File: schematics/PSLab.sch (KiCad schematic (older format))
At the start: 183 parts, among them J1 DoublePins, J11 Li-Ion Battery, J2 Power Pins, J3 Wave Generator, J4 I2C, J5 I2C, J6 ESP01, J7 UART, J9 SPI, P1 SDCard, Q1 MMBT3906, Q2 MMBT3904, Q3 MMBT3906, Q4 Q_NMOS_DGS, SW1 BOOT, SW2 MCLR Reset, SW3 USB_C - Generic, U1 LDFM33PUR, U10 TL082, U11 TL082, U12 MCP4728, U13 MCP6S21, U14 MCP6S21, U15 CP2102N, U16 SP0503BAHT, U18 LTC4040, U19 TC1240A, U2 74HC126, U3 PIC24EP256GP204, U4 DS1307Z+, U5 TC7660, U7 LM324, U8 TL082, U9 TL082, X2 32.768 kHz, Y1 12 MHz

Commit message: fix: osc signal routes
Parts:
- BT1: footprint Battery:BatteryHolder_LINX_BAT-HLD-012-SMT -> PSLab:BatteryHolder_LINX_BAT-HLD-012-SMT
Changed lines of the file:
@@
 Data
 89 50 4E 47 0D 0A 1A 0A 00 00 00 0D 49 48 44 52 00 00 02 08 00 00 00 CC 08 03 00 00 00 21 C4 AB
-DA 00 00 00 03 73 42 49 54 08 08 08 DB E1 4F E0 00 00 03 00 50 4C 54 45 02 00 00 FF FF E2 79 5D
+DA 00 00 00 03 73 42 49 54 08 08 08 DB E1 4F E0 00 00 03 00 50 4C 54 45 01 00 00 FF FF E2 79 5D
 9D 28 5D A5 28 7D CE E2 FF FF 81 5D B6 A5 EA FF C6 99 A5 28 99 E2 FF EA D6 59 5D C2 C6 FF FF 59
 B6 F2 FF FF F2 A5 7D A5 28 5D C6 E2 B6 B6 81 CE FF FF CE C6 81 7D D6 55 5D A1 59 7D BE F6 F6 F6
@@
 F6 99 D2 CE 40 9D D6 EA EE F6 40 5D A5 28 5D BA 7D D2 DE 55 AE DE 28 75 C2 CA DA EA 99 AA B6 65
 C2 DE 85 A5 CA 4C 4C 4C A1 A1 A1 3C 3C 3C 61 65 69 A5 B2 BE 85 A1 CE 91 99 A1 EE F2 F2 7D 81 81
-B6 BE C6 91 91 91 7D 7D 81 50 79 B6 C2 C2 C2 99 B2 7D 5D B6 DE FA FA FA 4A AB 90 C2 00 00 00 01
+B6 BE C6 91 91 91 7D 7D 81 50 79 B6 C2 C2 C2 99 B2 7D 5D B6 DE FA FA FA 76 CF DF 8C 00 00 00 01
 74 52 4E 53 00 40 E6 D8 66 00 00 15 08 49 44 41 54 78 9C ED 9D 7B 80 15 D5 79 C0 67 99 A5 31 A6
 26 05 83 EC 2E FB 76 60 9B 44 F6 01 BB CA 43 77 F7 C6 18 1F 10 31 36 1B 5D 4C 82 69 D6 24 D6 A0
@@
 F 0 "BT1" V 11150 7276 50  0000 C CNN
 F 1 "CR1225" V 11251 7086 50  0000 C CNN
-F 2 "Battery:BatteryHolder_LINX_BAT-HLD-012-SMT" V 11100 7085 50  0001 C CNN
+F 2 "PSLab:BatteryHolder_LINX_BAT-HLD-012-SMT" V 11100 7085 50  0001 C CNN
 F 3 "https://eu.mouser.com/datasheet/2/238/bat-hld-012-smt-1659340.pdf" V 11100 7085 50  0001 C CNN
 F 4 "Coin cell battery holder (CR1225/1216)" V 11100 7025 50  0001 C CNN "Description"

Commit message: refactor: global track refresh
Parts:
- U1: footprint Package_DFN_QFN:DFN-6-1EP_3x3mm_P0.95mm_EP1.7x2.6mm -> PSLab:DFN-6-1EP_3x3mm_P0.95mm_EP1.7x2.6mm
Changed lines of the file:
@@
 Data
 89 50 4E 47 0D 0A 1A 0A 00 00 00 0D 49 48 44 52 00 00 02 08 00 00 00 CC 08 03 00 00 00 21 C4 AB
-DA 00 00 00 03 73 42 49 54 08 08 08 DB E1 4F E0 00 00 03 00 50 4C 54 45 01 00 00 FF FF E2 79 5D
+DA 00 00 00 03 73 42 49 54 08 08 08 DB E1 4F E0 00 00 03 00 50 4C 54 45 02 00 00 FF FF E2 79 5D
 9D 28 5D A5 28 7D CE E2 FF FF 81 5D B6 A5 EA FF C6 99 A5 28 99 E2 FF EA D6 59 5D C2 C6 FF FF 59
 B6 F2 FF FF F2 A5 7D A5 28 5D C6 E2 B6 B6 81 CE FF FF CE C6 81 7D D6 55 5D A1 59 7D BE F6 F6 F6
@@
 F6 99 D2 CE 40 9D D6 EA EE F6 40 5D A5 28 5D BA 7D D2 DE 55 AE DE 28 75 C2 CA DA EA 99 AA B6 65
 C2 DE 85 A5 CA 4C 4C 4C A1 A1 A1 3C 3C 3C 61 65 69 A5 B2 BE 85 A1 CE 91 99 A1 EE F2 F2 7D 81 81
-B6 BE C6 91 91 91 7D 7D 81 50 79 B6 C2 C2 C2 99 B2 7D 5D B6 DE FA FA FA 76 CF DF 8C 00 00 00 01
+B6 BE C6 91 91 91 7D 7D 81 50 79 B6 C2 C2 C2 99 B2 7D 5D B6 DE FA FA FA 4A AB 90 C2 00 00 00 01
 74 52 4E 53 00 40 E6 D8 66 00 00 15 08 49 44 41 54 78 9C ED 9D 7B 80 15 D5 79 C0 67 99 A5 31 A6
 26 05 83 EC 2E FB 76 60 9B 44 F6 01 BB CA 43 77 F7 C6 18 1F 10 31 36 1B 5D 4C 82 69 D6 24 D6 A0
@@
 F 0 "U1" H 6900 4400 50  0000 C CNN
 F 1 "LDFM33PUR" H 7295 4400 50  0000 C CNN
-F 2 "Package_DFN_QFN:DFN-6-1EP_3x3mm_P0.95mm_EP1.7x2.6mm" H 7200 4200 60  0001 C CNN
+F 2 "PSLab:DFN-6-1EP_3x3mm_P0.95mm_EP1.7x2.6mm" H 7200 4200 60  0001 C CNN
 F 3 "https://eu.mouser.com/datasheet/2/389/dm00063302-1797750.pdf" H 7200 4200 60  0001 C CNN
 F 4 "DFN-6-1EP_3x3mm_Pitch0.95mm" H 7200 4200 50  0001 C CNN "Description"

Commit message: upgrade: lm324 to tssop14
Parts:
- U7: footprint Package_SO:SOIC-14_3.9x8.7mm_P1.27mm -> Package_SO:TSSOP-14_4.4x5mm_P0.65mm; Description SOIC 14 -> TSSOP-14; Mfr No. LM324D -> LM324APT; PartNumber LM324D -> LM324APT; Price (none) -> 0.45
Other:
- note added: "01"
- note added: "02"
- note added: "03"
- note added: "04"
- note added: "Oscilloscope Channel 01"
- note added: "Oscilloscope Channel 02"
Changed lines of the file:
@@
 Data
 89 50 4E 47 0D 0A 1A 0A 00 00 00 0D 49 48 44 52 00 00 02 08 00 00 00 CC 08 03 00 00 00 21 C4 AB
-DA 00 00 00 03 73 42 49 54 08 08 08 DB E1 4F E0 00 00 03 00 50 4C 54 45 02 00 00 FF FF E2 79 5D
+DA 00 00 00 03 73 42 49 54 08 08 08 DB E1 4F E0 00 00 03 00 50 4C 54 45 01 00 00 FF FF E2 79 5D
 9D 28 5D A5 28 7D CE E2 FF FF 81 5D B6 A5 EA FF C6 99 A5 28 99 E2 FF EA D6 59 5D C2 C6 FF FF 59
 B6 F2 FF FF F2 A5 7D A5 28 5D C6 E2 B6 B6 81 CE FF FF CE C6 81 7D D6 55 5D A1 59 7D BE F6 F6 F6
@@
 F6 99 D2 CE 40 9D D6 EA EE F6 40 5D A5 28 5D BA 7D D2 DE 55 AE DE 28 75 C2 CA DA EA 99 AA B6 65
 C2 DE 85 A5 CA 4C 4C 4C A1 A1 A1 3C 3C 3C 61 65 69 A5 B2 BE 85 A1 CE 91 99 A1 EE F2 F2 7D 81 81
-B6 BE C6 91 91 91 7D 7D 81 50 79 B6 C2 C2 C2 99 B2 7D 5D B6 DE FA FA FA 4A AB 90 C2 00 00 00 01
+B6 BE C6 91 91 91 7D 7D 81 50 79 B6 C2 C2 C2 99 B2 7D 5D B6 DE FA FA FA 76 CF DF 8C 00 00 00 01
 74 52 4E 53 00 40 E6 D8 66 00 00 15 08 49 44 41 54 78 9C ED 9D 7B 80 15 D5 79 C0 67 99 A5 31 A6
 26 05 83 EC 2E FB 76 60 9B 44 F6 01 BB CA 43 77 F7 C6 18 1F 10 31 36 1B 5D 4C 82 69 D6 24 D6 A0
@@
 F 0 "U7" H 21175 3075 50  0000 C CNN
 F 1 "LM324" H 21125 2900 50  0000 C CNN
-F 2 "Package_SO:SOIC-14_3.9x8.7mm_P1.27mm" H 21125 3000 50  0001 C CNN
-F 3 "http://www.ti.com/general/docs/suppproductinfo.tsp?distId=26&gotoUrl=http%3A%2F%2Fwww.ti.com%2Flit%2Fgpn%2FLM324" H 21225 3100 50  0001 C CNN
-F 4 "LM324D" H 21175 2900 50  0001 C CNN "PartNumber"
-F 5 "SOIC 14" H 21175 2900 50  0001 C CNN "Description"
-F 6 "LM324D" H 21175 2900 50  0001 C CNN "Mfr No."
+F 2 "Package_SO:TSSOP-14_4.4x5mm_P0.65mm" H 21125 3000 50  0001 C CNN
+F 3 "https://eu.mouser.com/datasheet/2/389/cd00001046-1795623.pdf" H 21225 3100 50  0001 C CNN
+F 4 "LM324APT" H 21175 2900 50  0001 C CNN "PartNumber"
+F 5 "TSSOP-14" H 21175 2900 50  0001 C CNN "Description"
+F 6 "LM324APT" H 21175 2900 50  0001 C CNN "Mfr No."
+F 7 "0.45" H 21175 2900 50  0001 C CNN "Price"
 	1    21175 2900
 	1    0    0    -1
@@
 F 0 "U7" H 21175 2100 50  0000 C CNN
 F 1 "LM324" H 21100 1925 50  0000 C CNN
-F 2 "Package_SO:SOIC-14_3.9x8.7mm_P1.27mm" H 21100 2025 50  0001 C CNN
-F 3 "http://www.ti.com/general/docs/suppproductinfo.tsp?distId=26&gotoUrl=http%3A%2F%2Fwww.ti.com%2Flit%2Fgpn%2FLM324" H 21200 2125 50  0001 C CNN
-F 4 "SOIC 14" H 21150 1925 50  0001 C CNN "Description"
-F 5 "LM324D" H 21150 1925 50  0001 C CNN "Mfr No."
-F 6 "LM324D" H 21150 1925 50  0001 C CNN "PartNumber"
+F 2 "Package_SO:TSSOP-14_4.4x5mm_P0.65mm" H 21100 2025 50  0001 C CNN
+F 3 "https://eu.mouser.com/datasheet/2/389/cd00001046-1795623.pdf" H 21200 2125 50  0001 C CNN
+F 4 "TSSOP-14" H 21150 1925 50  0001 C CNN "Description"
+F 5 "LM324APT" H 21150 1925 50  0001 C CNN "Mfr No."
+F 6 "LM324APT" H 21150 1925 50  0001 C CNN "PartNumber"
+F 7 "0.45" H 21150 1925 50  0001 C CNN "Price"
 	2    21150 1925
 	1    0    0    -1
@@
 F 0 "U7" H 21175 1175 50  0000 C CNN
 F 1 "LM324" H 21100 1350 50  0000 C CNN
-F 2 "Package_SO:SOIC-14_3.9x8.7mm_P1.27mm" H 21100 1450 50  0001 C CNN
-F 3 "http://www.ti.com/general/docs/suppproductinfo.tsp?distId=26&gotoUrl=http%3A%2F%2Fwww.ti.com%2Flit%2Fgpn%2FLM324" H 21200 1550 50  0001 C CNN
-F 4 "SOIC 14" H 21150 1350 50  0001 C CNN "Description"
-F 5 "LM324D" H 21150 1350 50  0001 C CNN "Mfr No."
-F 6 "LM324D" H 21150 1350 50  0001 C CNN "PartNumber"
+F 2 "Package_SO:TSSOP-14_4.4x5mm_P0.65mm" H 21100 1450 50  0001 C CNN
+F 3 "https://eu.mouser.com/datasheet/2/389/cd00001046-1795623.pdf" H 21200 1550 50  0001 C CNN
+F 4 "TSSOP-14" H 21150 1350 50  0001 C CNN "Description"
+F 5 "LM324APT" H 21150 1350 50  0001 C CNN "Mfr No."
+F 6 "LM324APT" H 21150 1350 50  0001 C CNN "PartNumber"
+F 7 "0.45" H 21150 1350 50  0001 C CNN "Price"
 	3    21150 1350
 	1    0    0    1
@@
 F 0 "U7" H 22050 3075 50  0000 C CNN
 F 1 "LM324" H 21975 2900 50  0000 C CNN
-F 2 "Package_SO:SOIC-14_3.9x8.7mm_P1.27mm" H 21975 3000 50  0001 C CNN
-F 3 "http://www.ti.com/general/docs/suppproductinfo.tsp?distId=26&gotoUrl=http%3A%2F%2Fwww.ti.com%2Flit%2Fgpn%2FLM324" H 22075 3100 50  0001 C CNN
-F 4 "SOIC 14" H 22025 2900 50  0001 C CNN "Description"
-F 5 "LM324D" H 22025 2900 50  0001 C CNN "Mfr No."
-F 6 "LM324D" H 22025 2900 50  0001 C CNN "PartNumber"
+F 2 "Package_SO:TSSOP-14_4.4x5mm_P0.65mm" H 21975 3000 50  0001 C CNN
+F 3 "https://eu.mouser.com/datasheet/2/389/cd00001046-1795623.pdf" H 22075 3100 50  0001 C CNN
+F 4 "TSSOP-14" H 22025 2900 50  0001 C CNN "Description"
+F 5 "LM324APT" H 22025 2900 50  0001 C CNN "Mfr No."
+F 6 "LM324APT" H 22025 2900 50  0001 C CNN "PartNumber"
+F 7 "0.45" H 22025 2900 50  0001 C CNN "Price"
 	4    22025 2900
 	1    0    0    -1
@@
 F 0 "U7" V 19525 2875 50  0000 C CNN
 F 1 "LM324" V 19800 2875 50  0000 C CNN
-F 2 "Package_SO:SOIC-14_3.9x8.7mm_P1.27mm" H 19725 2975 50  0001 C CNN
-F 3 "http://www.ti.com/general/docs/suppproductinfo.tsp?distId=26&gotoUrl=http%3A%2F%2Fwww.ti.com%2Flit%2Fgpn%2FLM324" H 19825 3075 50  0001 C CNN
-F 4 "SOIC 14" H 19775 2875 50  0001 C CNN "Description"
-F 5 "LM324D" H 19775 2875 50  0001 C CNN "Mfr No."
-F 6 "LM324D" H 19775 2875 50  0001 C CNN "PartNumber"
+F 2 "Package_SO:TSSOP-14_4.4x5mm_P0.65mm" H 19725 2975 50  0001 C CNN
+F 3 "https://eu.mouser.com/datasheet/2/389/cd00001046-1795623.pdf" H 19825 3075 50  0001 C CNN
+F 4 "TSSOP-14" H 19775 2875 50  0001 C CNN "Description"
+F 5 "LM324APT" H 19775 2875 50  0001 C CNN "Mfr No."
+F 6 "LM324APT" H 19775 2875 50  0001 C CNN "PartNumber"
+F 7 "0.45" H 19775 2875 50  0001 C CNN "Price"
 	5    19775 2875
 	0    1    1    0
@@
 	0    -1   -1   0
 $EndComp
+Text Notes 19000 6050 0    39   ~ 8
+Oscilloscope Channel 02
+Text Notes 15050 6050 0    39   ~ 8
+Oscilloscope Channel 01
+Text Notes 15075 8350 0    79   ~ 16
+01
+Wire Notes Line style solid rgb(255, 0, 0)
+	15025 8175 15300 8175
+Wire Notes Line style solid rgb(255, 0, 0)
+	15300 8175 15300 8425
+Text Notes 19025 8350 0    79   ~ 16
+02
+Wire Notes Line style solid rgb(255, 0, 0)
+	18975 8175 19250 8175
+Wire Notes Line style solid rgb(255, 0, 0)
+	19250 8175 19250 8425
+Text Notes 18475 5725 0    79   ~ 16
+03
+Wire Notes Line style solid rgb(255, 0, 0)
+	18425 5550 18700 5550
+Wire Notes Line style solid rgb(255, 0, 0)
+	18700 5550 18700 5800
+Text Notes 15075 5725 0    79   ~ 16
+04
+Wire Notes Line style solid rgb(255, 0, 0)
+	15025 5550 15300 5550
+Wire Notes Line style solid rgb(255, 0, 0)
+	15300 5550 15300 5800
 $EndSCHEMATC

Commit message: refactor: osc placement
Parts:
- U2: footprint Package_SO:SOIC-14_3.9x8.7mm_P1.27mm -> Package_SO:TSSOP-14_4.4x5mm_P0.65mm; Description (none) -> TSSOP-14; Mfr No. (none) -> SN74HC126PW; PartNumber (none) -> SN74HC126PW; Price (none) -> 0.42
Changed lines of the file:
@@
 F 0 "U2" H 10575 9492 39  0000 C CNN
 F 1 "74HC126" H 10575 9575 50  0000 C CNN
-F 2 "Package_SO:SOIC-14_3.9x8.7mm_P1.27mm" H 10575 9275 50  0001 C CNN
-F 3 "https://eu.mouser.com/datasheet/2/408/74HC126D_datasheet_en_20160804-959200.pdf" H 10575 9275 50  0001 C CNN
+F 2 "Package_SO:TSSOP-14_4.4x5mm_P0.65mm" H 10575 9275 50  0001 C CNN
+F 3 "http://www.ti.com/general/docs/suppproductinfo.tsp?distId=26&gotoUrl=http%3A%2F%2Fwww.ti.com%2Flit%2Fgpn%2Fsn74hc126" H 10575 9275 50  0001 C CNN
+F 4 "TSSOP-14" H 10575 9275 50  0001 C CNN "Description"
+F 5 "SN74HC126PW" H 10575 9275 50  0001 C CNN "Mfr No."
+F 6 "SN74HC126PW" H 10575 9275 50  0001 C CNN "PartNumber"
+F 7 "0.42" H 10575 9275 50  0001 C CNN "Price"
 	1    10575 9275
 	1    0    0    1
@@
 F 0 "U2" H 11725 9492 39  0000 C CNN
 F 1 "74HC126" H 11725 9575 50  0000 C CNN
-F 2 "Package_SO:SOIC-14_3.9x8.7mm_P1.27mm" H 11725 9275 50  0001 C CNN
-F 3 "https://eu.mouser.com/datasheet/2/408/74HC126D_datasheet_en_20160804-959200.pdf" H 11725 9275 50  0001 C CNN
+F 2 "Package_SO:TSSOP-14_4.4x5mm_P0.65mm" H 11725 9275 50  0001 C CNN
+F 3 "http://www.ti.com/general/docs/suppproductinfo.tsp?distId=26&gotoUrl=http%3A%2F%2Fwww.ti.com%2Flit%2Fgpn%2Fsn74hc126" H 11725 9275 50  0001 C CNN
+F 4 "TSSOP-14" H 11725 9275 50  0001 C CNN "Description"
+F 5 "SN74HC126PW" H 11725 9275 50  0001 C CNN "Mfr No."
+F 6 "SN74HC126PW" H 11725 9275 50  0001 C CNN "PartNumber"
+F 7 "0.42" H 11725 9275 50  0001 C CNN "Price"
 	2    11725 9275
 	1    0    0    1
@@
 F 0 "U2" H 11725 10617 39  0000 C CNN
 F 1 "74HC126" H 11725 10700 50  0000 C CNN
-F 2 "Package_SO:SOIC-14_3.9x8.7mm_P1.27mm" H 11725 10400 50  0001 C CNN
-F 3 "https://eu.mouser.com/datasheet/2/408/74HC126D_datasheet_en_20160804-959200.pdf" H 11725 10400 50  0001 C CNN
+F 2 "Package_SO:TSSOP-14_4.4x5mm_P0.65mm" H 11725 10400 50  0001 C CNN
+F 3 "http://www.ti.com/general/docs/suppproductinfo.tsp?distId=26&gotoUrl=http%3A%2F%2Fwww.ti.com%2Flit%2Fgpn%2Fsn74hc126" H 11725 10400 50  0001 C CNN
+F 4 "TSSOP-14" H 11725 10400 50  0001 C CNN "Description"
+F 5 "SN74HC126PW" H 11725 10400 50  0001 C CNN "Mfr No."
+F 6 "SN74HC126PW" H 11725 10400 50  0001 C CNN "PartNumber"
+F 7 "0.42" H 11725 10400 50  0001 C CNN "Price"
 	3    11725 10400
 	1    0    0    1
@@
 F 0 "U2" H 10575 10617 39  0000 C CNN
 F 1 "74HC126" H 10575 10700 50  0000 C CNN
-F 2 "Package_SO:SOIC-14_3.9x8.7mm_P1.27mm" H 10575 10400 50  0001 C CNN
-F 3 "https://eu.mouser.com/datasheet/2/408/74HC126D_datasheet_en_20160804-959200.pdf" H 10575 10400 50  0001 C CNN
+F 2 "Package_SO:TSSOP-14_4.4x5mm_P0.65mm" H 10575 10400 50  0001 C CNN
+F 3 "http://www.ti.com/general/docs/suppproductinfo.tsp?distId=26&gotoUrl=http%3A%2F%2Fwww.ti.com%2Flit%2Fgpn%2Fsn74hc126" H 10575 10400 50  0001 C CNN
+F 4 "TSSOP-14" H 10575 10400 50  0001 C CNN "Description"
+F 5 "SN74HC126PW" H 10575 10400 50  0001 C CNN "Mfr No."
+F 6 "SN74HC126PW" H 10575 10400 50  0001 C CNN "PartNumber"
+F 7 "0.42" H 10575 10400 50  0001 C CNN "Price"
 	4    10575 10400
 	1    0    0    1
@@
 F 0 "U2" H 9400 10200 39  0000 L CNN
 F 1 "74HC126" H 9425 9850 50  0000 L CNN
-F 2 "Package_SO:SOIC-14_3.9x8.7mm_P1.27mm" H 9600 9850 50  0001 C CNN
-F 3 "https://eu.mouser.com/datasheet/2/408/74HC126D_datasheet_en_20160804-959200.pdf" H 9600 9850 50  0001 C CNN
+F 2 "Package_SO:TSSOP-14_4.4x5mm_P0.65mm" H 9600 9850 50  0001 C CNN
+F 3 "http://www.ti.com/general/docs/suppproductinfo.tsp?distId=26&gotoUrl=http%3A%2F%2Fwww.ti.com%2Flit%2Fgpn%2Fsn74hc126" H 9600 9850 50  0001 C CNN
+F 4 "TSSOP-14" H 9600 9850 50  0001 C CNN "Description"
+F 5 "SN74HC126PW" H 9600 9850 50  0001 C CNN "Mfr No."
+F 6 "SN74HC126PW" H 9600 9850 50  0001 C CNN "PartNumber"
+F 7 "0.42" H 9600 9850 50  0001 C CNN "Price"
 	5    9600 9850
 	1    0    0    -1

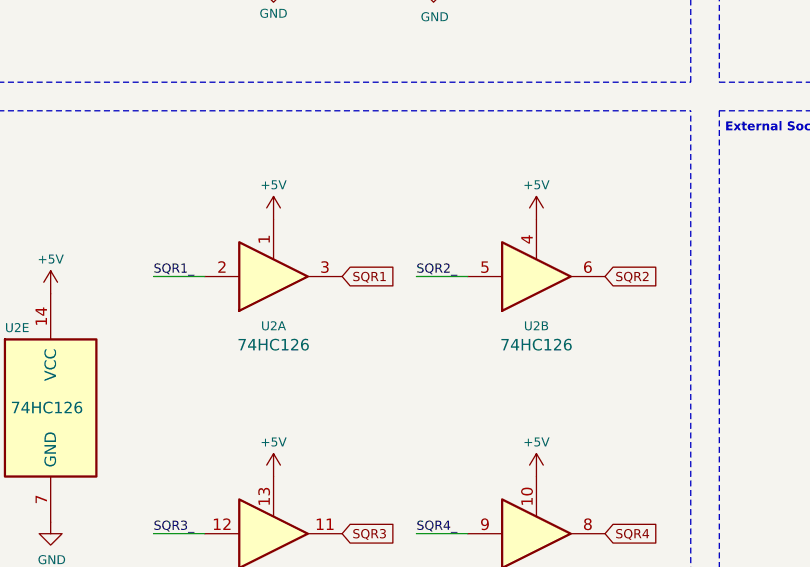
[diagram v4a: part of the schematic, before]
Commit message: refactor: wave generator circuit
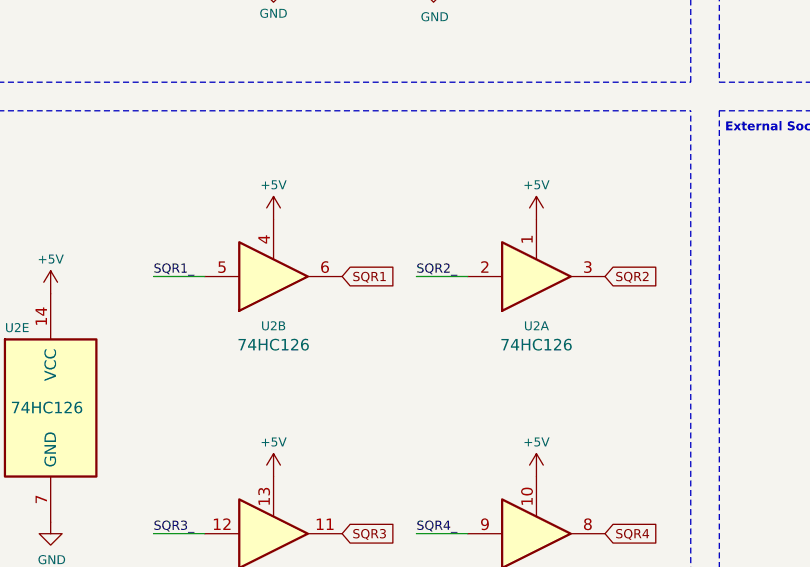
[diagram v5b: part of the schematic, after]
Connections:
- net SQR1: now also U2.6; no longer U2.3
- net SQR1_: now also U2.5; no longer U2.2
- net SQR2: now also U2.3; no longer U2.6
- net SQR2_: now also U2.2; no longer U2.5
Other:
- moved on the sheet: U2A, U2B
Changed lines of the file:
@@
 Data
 89 50 4E 47 0D 0A 1A 0A 00 00 00 0D 49 48 44 52 00 00 02 08 00 00 00 CC 08 03 00 00 00 21 C4 AB
-DA 00 00 00 03 73 42 49 54 08 08 08 DB E1 4F E0 00 00 03 00 50 4C 54 45 01 00 00 FF FF E2 79 5D
+DA 00 00 00 03 73 42 49 54 08 08 08 DB E1 4F E0 00 00 03 00 50 4C 54 45 02 00 00 FF FF E2 79 5D
 9D 28 5D A5 28 7D CE E2 FF FF 81 5D B6 A5 EA FF C6 99 A5 28 99 E2 FF EA D6 59 5D C2 C6 FF FF 59
 B6 F2 FF FF F2 A5 7D A5 28 5D C6 E2 B6 B6 81 CE FF FF CE C6 81 7D D6 55 5D A1 59 7D BE F6 F6 F6
@@
 F6 99 D2 CE 40 9D D6 EA EE F6 40 5D A5 28 5D BA 7D D2 DE 55 AE DE 28 75 C2 CA DA EA 99 AA B6 65
 C2 DE 85 A5 CA 4C 4C 4C A1 A1 A1 3C 3C 3C 61 65 69 A5 B2 BE 85 A1 CE 91 99 A1 EE F2 F2 7D 81 81
-B6 BE C6 91 91 91 7D 7D 81 50 79 B6 C2 C2 C2 99 B2 7D 5D B6 DE FA FA FA 76 CF DF 8C 00 00 00 01
+B6 BE C6 91 91 91 7D 7D 81 50 79 B6 C2 C2 C2 99 B2 7D 5D B6 DE FA FA FA 4A AB 90 C2 00 00 00 01
 74 52 4E 53 00 40 E6 D8 66 00 00 15 08 49 44 41 54 78 9C ED 9D 7B 80 15 D5 79 C0 67 99 A5 31 A6
 26 05 83 EC 2E FB 76 60 9B 44 F6 01 BB CA 43 77 F7 C6 18 1F 10 31 36 1B 5D 4C 82 69 D6 24 D6 A0
@@
 L 74xx:74LS126 U2
 U 1 1 60F1406B
+P 11725 9275
+F 0 "U2" H 11725 9492 39  0000 C CNN
+F 1 "74HC126" H 11725 9575 50  0000 C CNN
+F 2 "Package_SO:TSSOP-14_4.4x5mm_P0.65mm" H 11725 9275 50  0001 C CNN
+F 3 "http://www.ti.com/general/docs/suppproductinfo.tsp?distId=26&gotoUrl=http%3A%2F%2Fwww.ti.com%2Flit%2Fgpn%2Fsn74hc126" H 11725 9275 50  0001 C CNN
+F 4 "TSSOP-14" H 11725 9275 50  0001 C CNN "Description"
+F 5 "SN74HC126PW" H 11725 9275 50  0001 C CNN "Mfr No."
+F 6 "SN74HC126PW" H 11725 9275 50  0001 C CNN "PartNumber"
+F 7 "0.42" H 11725 9275 50  0001 C CNN "Price"
+	1    11725 9275
+	1    0    0    1
+$EndComp
+$Comp
+L 74xx:74LS126 U2
+U 2 1 60F15995
 P 10575 9275
 F 0 "U2" H 10575 9492 39  0000 C CNN
@@
 F 6 "SN74HC126PW" H 10575 9275 50  0001 C CNN "PartNumber"
 F 7 "0.42" H 10575 9275 50  0001 C CNN "Price"
-	1    10575 9275
+	2    10575 9275
 	1    0    0    1
 $EndComp
-$Comp
-L 74xx:74LS126 U2
-U 2 1 60F15995
-P 11725 9275
-F 0 "U2" H 11725 9492 39  0000 C CNN
-F 1 "74HC126" H 11725 9575 50  0000 C CNN
-F 2 "Package_SO:TSSOP-14_4.4x5mm_P0.65mm" H 11725 9275 50  0001 C CNN
-F 3 "http://www.ti.com/general/docs/suppproductinfo.tsp?distId=26&gotoUrl=http%3A%2F%2Fwww.ti.com%2Flit%2Fgpn%2Fsn74hc126" H 11725 9275 50  0001 C CNN
-F 4 "TSSOP-14" H 11725 9275 50  0001 C CNN "Description"
-F 5 "SN74HC126PW" H 11725 9275 50  0001 C CNN "Mfr No."
-F 6 "SN74HC126PW" H 11725 9275 50  0001 C CNN "PartNumber"
-F 7 "0.42" H 11725 9275 50  0001 C CNN "Price"
-	2    11725 9275
-	1    0    0    1
-$EndComp

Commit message: refactor: initial routing
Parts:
- Q4: footprint Package_SO:PowerPAK_SO-8_Single -> PSLab:PowerPAK_SO-8_Single; Description (none) -> MOSFET 20V Vds 20V Vgs PowerPAK SO-8; Mfr No. (none) -> SIR424DP-T1-GE3; Price (none) -> 0.99
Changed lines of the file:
@@
 F 0 "Q4" H 3550 5300 39  0000 L CNN
 F 1 "Q_NMOS_DGS" V 3900 4950 39  0000 L CNN
-F 2 "Package_SO:PowerPAK_SO-8_Single" H 3850 5250 50  0001 C CNN
-F 3 "~" H 3650 5150 50  0001 C CNN
+F 2 "PSLab:PowerPAK_SO-8_Single" H 3850 5250 50  0001 C CNN
+F 3 "https://www.mouser.fi/datasheet/2/427/sir424dp-1765120.pdf" H 3650 5150 50  0001 C CNN
 F 4 "SIR424DP-T1-GE3" H 3650 5150 50  0001 C CNN "PartNumber"
+F 5 "SIR424DP-T1-GE3" H 3650 5150 50  0001 C CNN "Mfr No."
+F 6 "0.99" H 3650 5150 50  0001 C CNN "Price"
+F 7 "MOSFET 20V Vds 20V Vgs PowerPAK SO-8" H 3650 5150 50  0001 C CNN "Description"
 	1    3650 5150
 	1    0    0    -1
@@
 Data
 89 50 4E 47 0D 0A 1A 0A 00 00 00 0D 49 48 44 52 00 00 02 08 00 00 00 CC 08 03 00 00 00 21 C4 AB
-DA 00 00 00 03 73 42 49 54 08 08 08 DB E1 4F E0 00 00 03 00 50 4C 54 45 02 00 00 FF FF E2 79 5D
+DA 00 00 00 03 73 42 49 54 08 08 08 DB E1 4F E0 00 00 03 00 50 4C 54 45 01 00 00 FF FF E2 79 5D
 9D 28 5D A5 28 7D CE E2 FF FF 81 5D B6 A5 EA FF C6 99 A5 28 99 E2 FF EA D6 59 5D C2 C6 FF FF 59
 B6 F2 FF FF F2 A5 7D A5 28 5D C6 E2 B6 B6 81 CE FF FF CE C6 81 7D D6 55 5D A1 59 7D BE F6 F6 F6
@@
 F6 99 D2 CE 40 9D D6 EA EE F6 40 5D A5 28 5D BA 7D D2 DE 55 AE DE 28 75 C2 CA DA EA 99 AA B6 65
 C2 DE 85 A5 CA 4C 4C 4C A1 A1 A1 3C 3C 3C 61 65 69 A5 B2 BE 85 A1 CE 91 99 A1 EE F2 F2 7D 81 81
-B6 BE C6 91 91 91 7D 7D 81 50 79 B6 C2 C2 C2 99 B2 7D 5D B6 DE FA FA FA 4A AB 90 C2 00 00 00 01
+B6 BE C6 91 91 91 7D 7D 81 50 79 B6 C2 C2 C2 99 B2 7D 5D B6 DE FA FA FA 76 CF DF 8C 00 00 00 01
 74 52 4E 53 00 40 E6 D8 66 00 00 15 08 49 44 41 54 78 9C ED 9D 7B 80 15 D5 79 C0 67 99 A5 31 A6
 26 05 83 EC 2E FB 76 60 9B 44 F6 01 BB CA 43 77 F7 C6 18 1F 10 31 36 1B 5D 4C 82 69 D6 24 D6 A0
